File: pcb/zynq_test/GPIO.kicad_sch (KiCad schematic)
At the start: 0 parts

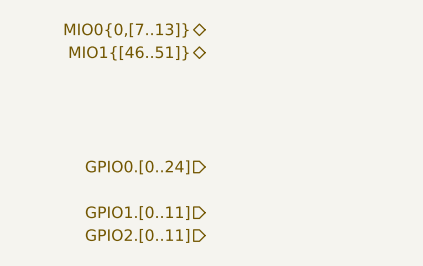
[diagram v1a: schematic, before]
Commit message: Finished to first ddr ic
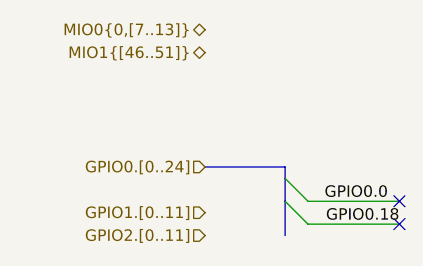
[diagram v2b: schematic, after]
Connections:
- no-connect marks 0 -> 2
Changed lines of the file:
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@@
 		(rev "A")
+	)
+	(no_connect
+		(at 66.04 78.74)
+	)
+	(no_connect
+		(at 66.04 81.28)
+	)
+	(bus_entry
+		(at 53.34 78.74)
+		(size 2.54 2.54)
+		(stroke
+			(width 0)
+			(type default)
+		)
+	)
+	(bus_entry
+		(at 53.34 76.2)
+		(size 2.54 2.54)
+		(stroke
+			(width 0)
+			(type default)
+		)
+	)
+	(wire
+		(pts
+			(xy 55.88 78.74) (xy 66.04 78.74)
+		)
+		(stroke
+			(width 0)
+			(type default)
+		)
+	)
+	(bus
+		(pts
+			(xy 53.34 78.74) (xy 53.34 82.55)
+		)
+		(stroke
+			(width 0)
+			(type default)
+		)
+	)
+	(bus
+		(pts
+			(xy 53.34 76.2) (xy 53.34 78.74)
+		)
+		(stroke
+			(width 0)
+			(type default)
+		)
+	)
+	(bus
+		(pts
+			(xy 53.34 74.93) (xy 53.34 76.2)
+		)
+		(stroke
+			(width 0)
+			(type default)
+		)
+	)
+	(bus
+		(pts
+			(xy 44.45 74.93) (xy 53.34 74.93)
+		)
+		(stroke
+			(width 0)
+			(type default)
+		)
+	)
+	(wire
+		(pts
+			(xy 55.88 81.28) (xy 66.04 81.28)
+		)
+		(stroke
+			(width 0)
+			(type default)
+		)
+	)
+	(label "GPIO0.0"
+		(at 64.77 78.74 180)
+		(effects
+			(font
+				(size 1.27 1.27)
+			)
+			(justify right bottom)
+		)
+	)
+	(label "GPIO0.18"
+		(at 66.04 81.28 180)
+		(effects
+			(font
+				(size 1.27 1.27)
+			)
+			(justify right bottom)
+		)
 	)
 	(hierarchical_label "MIO0{0,[7..13]}"

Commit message: Almost done with BOM
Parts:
- added C1301, C1302, C1303, C1304: 100n, Capacitor_SMD:C_0402_1005Metric, symbol Device:C
- added D1301: RED, LED_SMD:LED_0805_2012Metric, symbol Device:LED
- added D1302: GREEN, LED_SMD:LED_0805_2012Metric, symbol Device:LED
- added J1301, J1302: Conn_02x05_Odd_Even, Connector_PinSocket_2.54mm:PinSocket_2x05_P2.54mm_Horizontal, symbol Connector_Generic:Conn_01x10
- added J1303: Conn_01x06, Connector_PinHeader_2.54mm:PinHeader_1x06_P2.54mm_Vertical, symbol Connector_Generic:Conn_01x06
- added Q1301, Q1302: 2N7002E, Package_TO_SOT_SMD:SOT-23, symbol Transistor_FET:2N7002E
- added R1301, R1302: 10k, Resistor_SMD:R_0402_1005Metric, symbol Device:R_US
- added R1303, R1304: 220R, Resistor_SMD:R_0402_1005Metric, symbol Device:R_Small_US
- added U1301, U1302: FXMA108, Package_DFN_QFN:WQFN-20-1EP_2.5x4.5mm_P0.5mm_EP1x2.9mm, symbol Logic_LevelTranslator:FXMA108
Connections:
- new net: R1302.1, U1302.11 (~{OE})
- new net: D1302.1 (K), R1304.1
- new net: D1301.1 (K), R1303.1
- new net: Q1301.3 (D), R1303.2
- new net: R1301.1, U1301.11 (~{OE})
- new net: Q1302.3 (D), R1304.2
- new net +1V8: C1301.1, C1303.1, J1303.2 (Pin_2), U1301.1 (VCCA), U1302.1 (VCCA)
- new net +3V3: C1302.1, D1301.2 (A), D1302.2 (A), J1301.2 (Pin_2), J1303.1 (Pin_1), U1301.20 (VCCB)
- new net +5V: C1304.1, J1302.2 (Pin_2), U1302.20 (VCCB)
- new net GND: C1301.2, C1302.2, C1303.2, C1304.2, J1301.1 (Pin_1), J1302.1 (Pin_1), J1303.3 (Pin_3), Q1301.2 (S), Q1302.2 (S), R1301.2, R1302.2, U1301.10 (GND), U1302.10 (GND)
- new net GPIO0.11: U1301.3 (A1)
- new net GPIO0.12: U1301.5 (A3)
- new net GPIO0.15: U1302.3 (A1)
- new net GPIO0.16: U1301.8 (A6)
- new net GPIO0.19: U1301.9 (A7)
- new net GPIO0.21: U1302.2 (A0)
- new net GPIO0.23: U1301.2 (A0)
- new net GPIO0.5: U1301.4 (A2)
- new net GPIO0.7: U1301.6 (A4)
- new net GPIO0.8: U1301.7 (A5)
- new net GPIO0.OUT.11: J1301.8 (Pin_8), U1301.18 (B1)
- new net GPIO0.OUT.15: J1302.3 (Pin_3), U1302.18 (B1)
- new net GPIO0.OUT.16: J1301.3 (Pin_3), U1301.13 (B6)
- new net GPIO0.OUT.19: J1301.6 (Pin_6), U1301.12 (B7)
- new net GPIO0.OUT.21: J1302.4 (Pin_4), U1302.19 (B0)
- new net GPIO0.OUT.23: J1301.7 (Pin_7), U1301.19 (B0)
- new net GPIO0.OUT.5: J1301.9 (Pin_9), U1301.17 (B2)
- new net GPIO0.OUT.6: J1301.10 (Pin_10), U1301.16 (B3)
- new net GPIO0.OUT.7: J1301.5 (Pin_5), U1301.15 (B4)
- new net GPIO0.OUT.8: J1301.4 (Pin_4), U1301.14 (B5)
- new net GPIO1.9: U1302.4 (A2)
- new net GPIO1.OUT.9: J1302.6 (Pin_6), U1302.17 (B2)
- new net GPIO2.5: Q1301.1 (G)
- new net GPIO2.6: U1302.5 (A3)
- new net GPIO2.8: Q1302.1 (G)
- new net GPIO2.OUT.6: J1302.5 (Pin_5), U1302.16 (B3)
- new net MIO1.48: J1303.6 (Pin_6)
- new net MIO1.49: J1303.4 (Pin_4)
- new net MIO1.50: J1303.5 (Pin_5)
- no-connect marks 2 -> 51
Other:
- note added: "Bottom Connectors"
- note added: "Right LEDS"

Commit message: Version sent to JLCPCB
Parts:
- C1301, C1302, C1303, C1304: JLCPCB Part# (none) -> C1525; PART_NUMBER (none) -> CL05B104KO5NNNC
- D1301: JLCPCB Part# (none) -> C84256; PART_NUMBER (none) -> NCD0805R1
- D1302: JLCPCB Part# (none) -> C192672; PART_NUMBER (none) -> TJ-S2012SW8TGLC7K-A5
- J1301, J1302, J1303: now left out of the parts list
- Q1301, Q1302: JLCPCB Part# (none) -> C71533; PART_NUMBER (none) -> 2N7002E
- R1301, R1302: JLCPCB Part# (none) -> C191123; PART_NUMBER (none) -> ERJ2RKF1002X
- R1303, R1304: JLCPCB Part# (none) -> C412979; PART_NUMBER (none) -> ERJ2GEJ221X
- U1301, U1302: JLCPCB Part# (none) -> C891320; PART_NUMBER (none) -> FXMA108BQX
